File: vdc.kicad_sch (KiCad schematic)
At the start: 9 parts, among them IC102 HUC6270

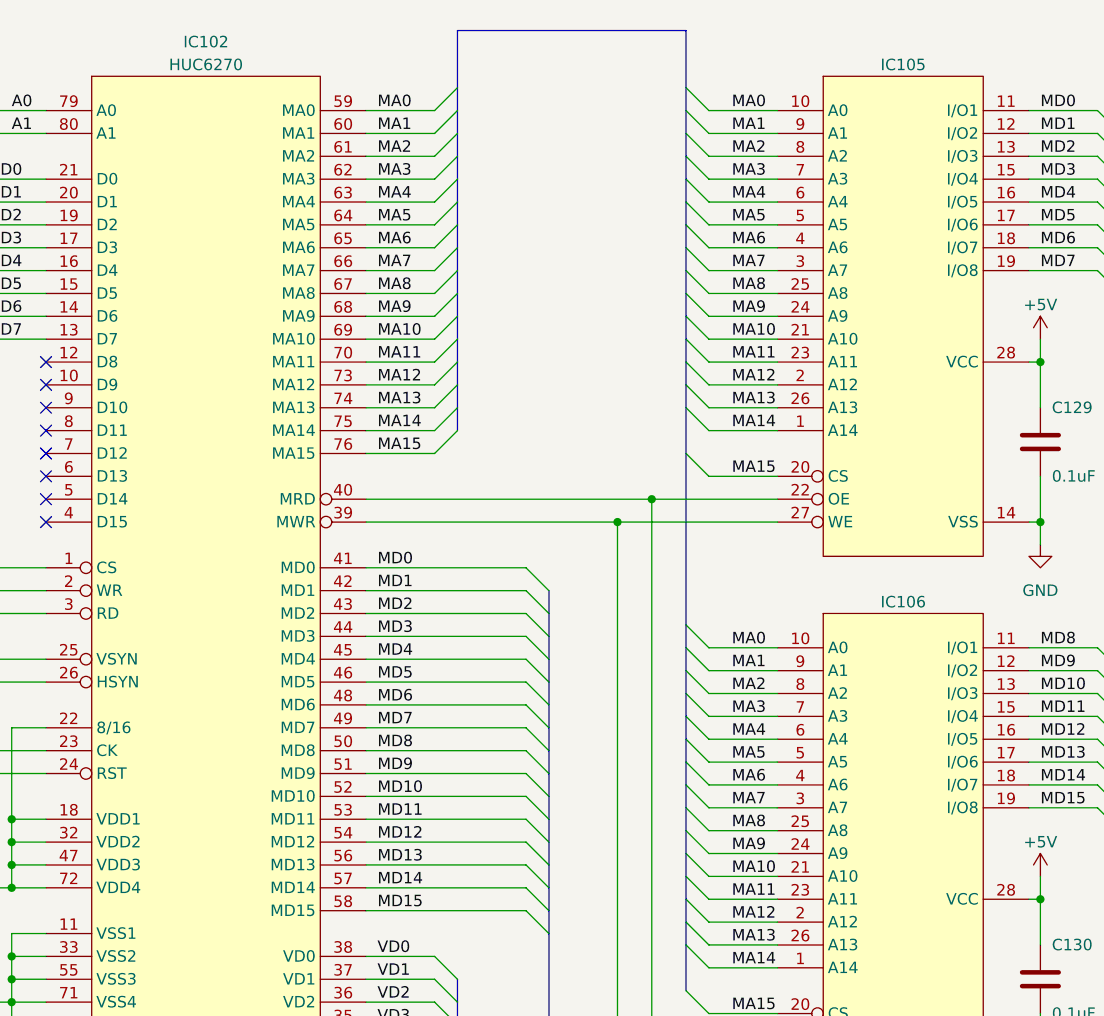
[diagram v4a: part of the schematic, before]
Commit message: Silkscreen stuff, tidy schematics, corrections.
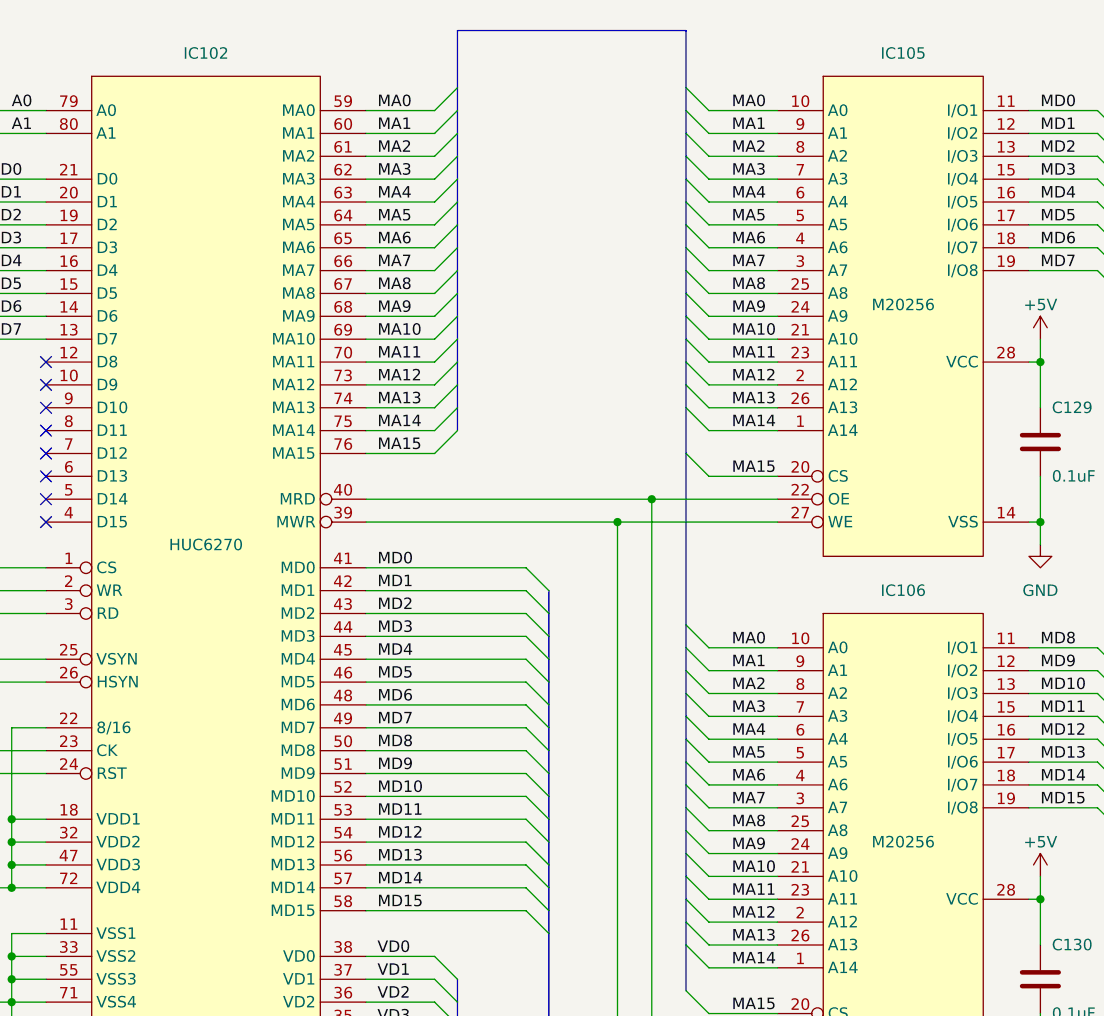
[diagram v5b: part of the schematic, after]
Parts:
- IC105, IC106: value ~ -> M20256
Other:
- title: (none) -> PC Engine Video Display Controller and VRAM
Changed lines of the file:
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@@
 (kicad_sch (version 20230121) (generator eeschema)
   (paper "A3")
+  (title_block
+    (title "PC Engine Video Display Controller and VRAM")
+    (date "2023-08-17")
+    (rev "1.0")
+    (comment 1 "Differences reverse engineered from original PWD-623A board")
+    (comment 2 "Adapted from existing TurboGrafx-16 schematics by Cosam")
+  )
   (junction (at 218.44 195.58) (diameter 0) (color 0 0 0 0)
   )
@@
   )
   (symbol (lib_id "PC-Engine:M20256") (at 261.62 97.79 0) (unit 1)
-    (in_bom yes) (on_board yes) (dnp no) (fields_autoplaced)
-    (property "Reference" "IC106" (at 261.62 99.06 0)
+    (in_bom yes) (on_board yes) (dnp no)
+    (property "Reference" "IC106" (at 261.62 97.79 0)
       (effects (font (size 1.27 1.27)))
     )
-    (property "Value" "~" (at 261.62 97.79 0)
+    (property "Value" "M20256" (at 261.62 125.73 0)
       (effects (font (size 1.27 1.27)))
     )
@@
   )
   (symbol (lib_id "PC-Engine:Hu6270") (at 184.15 100.33 0) (unit 1)
-    (in_bom yes) (on_board yes) (dnp no) (fields_autoplaced)
-    (property "Reference" "IC102" (at 184.15 36.83 0)
+    (in_bom yes) (on_board yes) (dnp no)
+    (property "Reference" "IC102" (at 184.15 38.1 0)
       (effects (font (size 1.27 1.27)))
     )
-    (property "Value" "HUC6270" (at 184.15 39.37 0)
+    (property "Value" "HUC6270" (at 184.15 92.71 0)
       (effects (font (size 1.27 1.27)))
     )
@@
   (symbol (lib_id "PC-Engine:M20256") (at 261.62 38.1 0) (unit 1)
     (in_bom yes) (on_board yes) (dnp no)
-    (property "Reference" "IC105" (at 261.62 39.37 0)
+    (property "Reference" "IC105" (at 261.62 38.1 0)
       (effects (font (size 1.27 1.27)))
     )
-    (property "Value" "~" (at 261.62 38.1 0)
+    (property "Value" "M20256" (at 261.62 66.04 0)
       (effects (font (size 1.27 1.27)))
     )
